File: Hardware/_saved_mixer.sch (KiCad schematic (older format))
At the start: 62 parts, among them J2 Audio-Jack-2_Switch, U3 TL074, U6 PT2399

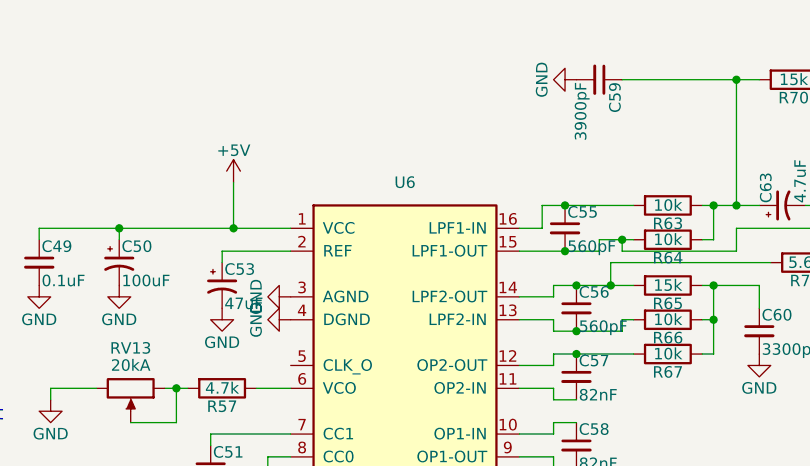
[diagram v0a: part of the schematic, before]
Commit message: begin PCB v2 layout. fix ref designators, associate footprints on new components, create new PCB file, import components.
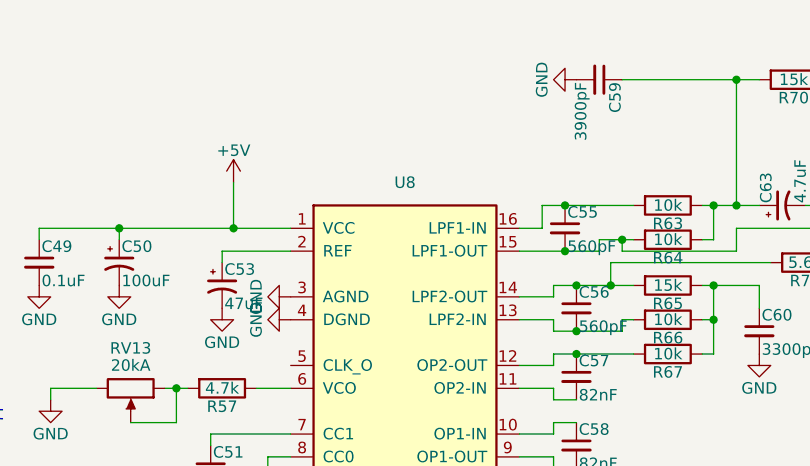
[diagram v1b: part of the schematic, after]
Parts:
- C49, C51, C54, C55, C56, C57, C58, C59, C60, C64: footprint (none) -> digikey-footprints:0805
- C50: footprint (none) -> Capacitors_SMD:CP_Elec_5x5.7
- C53, C63, C65, C66, C67: footprint (none) -> Capacitors_SMD:CP_Elec_4x5.7
- renumbered U6 to U8
